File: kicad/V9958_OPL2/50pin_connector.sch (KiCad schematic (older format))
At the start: 1 part, among them P5 CONN_02X25

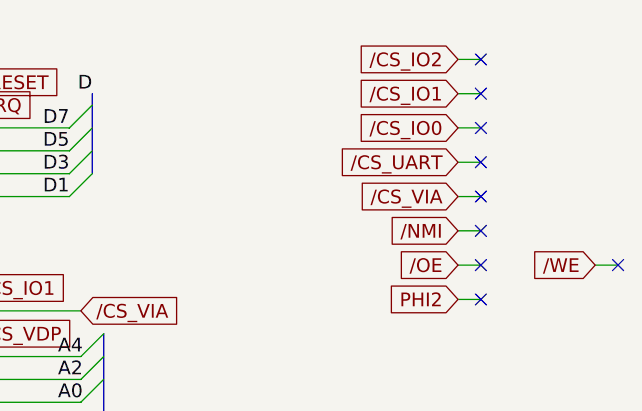
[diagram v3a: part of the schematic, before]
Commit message: DRC fixes, filled areas
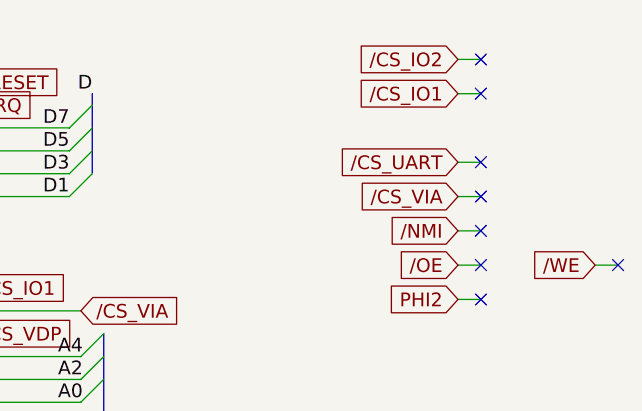
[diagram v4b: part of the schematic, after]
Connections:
- no-connect marks 17 -> 16
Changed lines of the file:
@@
 Text GLabel 8000 2600 0    60   Input ~ 0
 /CS_IO1
-Text GLabel 8000 2750 0    60   Input ~ 0
-/CS_IO0
 Wire Wire Line
 	8000 2450 8100 2450
 Wire Wire Line
 	8000 2600 8100 2600
-Wire Wire Line
-	8000 2750 8100 2750
 NoConn ~ 8100 2450
 NoConn ~ 8100 2600
-NoConn ~ 8100 2750
 Text GLabel 8000 2900 0    60   Input ~ 0
 /CS_UART
